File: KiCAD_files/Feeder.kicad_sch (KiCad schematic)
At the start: 82 parts, among them J405 Conn_01x02_Male, J406 Conn_01x02_Male, J501 Conn_01x03, Q501 60V N channel, Q502 TK13P25D,RQ, T501 PA2467NL, U407 OPA316, U501 NCP12700, U502 FODM217A, U503 TL431MFDT,215

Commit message: cleaned refdes
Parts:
- removed C415: 100nF, Footprints:C_0805_2012Metric, symbol Device:C_Small
- removed C503, C504, C505, C506: 4.7uF, Footprints:C_1210_3225Metric, symbol Device:C
- removed C509: 1nF, Footprints:C_0805_2012Metric, symbol Device:C
- removed C512, C513: 1uF, Footprints:C_0805_2012Metric, symbol Device:C
- removed C519: 10uF, Footprints:C_1210_3225Metric, symbol Device:C
- removed R422: 47k, Footprints:R_0805_2012Metric, symbol Device:R
- removed R423: 12k, Footprints:R_0805_2012Metric, symbol Device:R
- removed R502, R518: 27k, Footprints:R_0805_2012Metric, symbol Device:R
- removed R506: 470R, Footprints:R_0805_2012Metric, symbol Device:R
- removed U502: FODM217A, Package_SO:SO-4_4.4x2.3mm_P1.27mm, symbol Isolator:SFH617A-1X007T
- added C? (x2): 1uF, Footprints:C_0805_2012Metric, symbol Device:C_Small
- added C? (x4): 4.7uF, Footprints:C_1210_3225Metric, symbol Device:C
- added C?: 100nF, Footprints:C_0805_2012Metric, symbol Device:C_Small
- added C?: 10uF, Footprints:C_1210_3225Metric, symbol Device:C_Small
- added C?: 1nF, Footprints:C_0805_2012Metric, symbol Device:C_Small
- added R617: 470R, Footprints:R_0805_2012Metric, symbol Device:R_Small
- added R?: 12k, Footprints:R_0805_2012Metric, symbol Device:R_Small
- added R? (x2): 27k, Footprints:R_0805_2012Metric, symbol Device:R_Small
- added R?: 47k, Footprints:R_0805_2012Metric, symbol Device:R_Small
- added U?: FODM217A, Package_SO:SO-4_4.4x2.3mm_P1.27mm, symbol Isolator:SFH617A-2X009T
- C511: value X7T, 100nF -> 100nF; Dielectric (none) -> X7T
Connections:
- net +5V_DGND: now also C?.1, R?.2
- net +6VJP: now also C?.1
- net COMP: now also C?.2, U?.4
- net DGND: now also C?.2, C?.2, R?.1, R?.1
- net MOSS: now also R617.2
- net PGND: now also C?.1, C?.2, C?.2, C?.2, C?.2, R?.1, U?.3
- net VAUX: now also C?.1
- net VBoost: now also C?.1
- net input: now also C?.1, C?.1
- net at C520.2, R517.2, U503.2 (REF): now also R?.2
- net at C414.2, U407.1 (+): now also R?.1, R?.2
- net at R501.2, U501.1 (UVLO): now also R?.2
- net at R514.2, R515.1: now also U?.1
- net at C520.1, R515.2, U503.1 (K): now also U?.2
- net at C510.1, U501.6 (CS): now also R617.1
- new net: C?.1, C?.1, C?.2, C?.2

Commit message: changed LDO 10uF refdes so it is the same as on SPIN
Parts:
- C? (x5): Voltage 50V -> 25V; manf# 12105C106KAT2A -> CL21B106KAYQNNE
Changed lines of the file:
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@@
       (effects (font (size 1.27 1.27)) hide)
     )
-    (property "manf#" "12105C106KAT2A" (at 237.49 251.46 0)
+    (property "manf#" "CL21B106KAYQNNE" (at 237.49 251.46 0)
       (effects (font (size 1.27 1.27)) hide)
     )
@@
       (effects (font (size 1.27 1.27)) hide)
     )
-    (property "Voltage" "50V" (at 237.49 251.46 0)
+    (property "Voltage" "25V" (at 237.49 251.46 0)
       (effects (font (size 1.27 1.27)) hide)
     )
@@
       (effects (font (size 1.27 1.27)) hide)
     )
-    (property "manf#" "12105C106KAT2A" (at 196.85 251.46 0)
+    (property "manf#" "CL21B106KAYQNNE" (at 196.85 251.46 0)
       (effects (font (size 1.27 1.27)) hide)
     )
@@
       (effects (font (size 1.27 1.27)) hide)
     )
-    (property "Voltage" "50V" (at 196.85 251.46 0)
+    (property "Voltage" "25V" (at 196.85 251.46 0)
       (effects (font (size 1.27 1.27)) hide)
     )
@@
       (effects (font (size 1.27 1.27)) hide)
     )
-    (property "manf#" "12105C106KAT2A" (at 182.88 251.46 0)
+    (property "manf#" "CL21B106KAYQNNE" (at 182.88 251.46 0)
       (effects (font (size 1.27 1.27)) hide)
     )
@@
       (effects (font (size 1.27 1.27)) hide)
     )
-    (property "Voltage" "50V" (at 182.88 251.46 0)
+    (property "Voltage" "25V" (at 182.88 251.46 0)
       (effects (font (size 1.27 1.27)) hide)
     )
@@
       (effects (font (size 1.27 1.27)) hide)
     )
-    (property "manf#" "12105C106KAT2A" (at 137.16 250.19 0)
+    (property "manf#" "CL21B106KAYQNNE" (at 137.16 250.19 0)
       (effects (font (size 1.27 1.27)) hide)
     )
@@
       (effects (font (size 1.27 1.27)) hide)
     )
-    (property "Voltage" "50V" (at 137.16 250.19 0)
+    (property "Voltage" "25V" (at 137.16 250.19 0)
       (effects (font (size 1.27 1.27)) hide)
     )
@@
       (effects (font (size 1.27 1.27)) hide)
     )
-    (property "manf#" "12105C106KAT2A" (at 163.83 250.19 0)
+    (property "manf#" "CL21B106KAYQNNE" (at 163.83 250.19 0)
       (effects (font (size 1.27 1.27)) hide)
     )
@@
       (effects (font (size 1.27 1.27)) hide)
     )
-    (property "Voltage" "50V" (at 163.83 250.19 0)
+    (property "Voltage" "25V" (at 163.83 250.19 0)
       (effects (font (size 1.27 1.27)) hide)
     )

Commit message: Version as built for SN001 and SN002
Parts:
- removed R?: 27k, Footprints:R_0805_2012Metric, symbol Device:R_Small
- added R502: 14,7K, Footprints:R_0805_2012Metric, symbol Device:R
- C? (x2): Voltage 25V -> 50V; manf# CL21B106KAYQNNE -> 12105C106KAT2A
- R501: value 348k -> 147K; Package 0805 -> (none); Ref (none) -> ok; manf# CR0805-FX-3483ELF -> CR0805-FX-1473ELF
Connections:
- net PGND: now also R502.2
- net at R501.2, U501.1 (UVLO): now also R502.1
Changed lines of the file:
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@@
   (junction (at 172.72 243.84) (diameter 0) (color 0 0 0 0)
   )
+  (junction (at 77.47 74.93) (diameter 0) (color 0 0 0 0)
+  )
   (junction (at 156.21 60.96) (diameter 0) (color 0 0 0 0)
   )
   (junction (at 198.12 71.12) (diameter 0) (color 0 0 0 0)
   )
-  (junction (at 77.47 74.93) (diameter 0) (color 0 0 0 0)
-  )
   (junction (at 201.93 46.99) (diameter 0) (color 0 0 0 0)
   )
@@
     (stroke (width 0.5) (type default))
   )
+  (wire (pts (xy 77.47 74.93) (xy 77.47 87.63))
+    (stroke (width 0) (type default))
+  )
   (wire (pts (xy 181.61 93.98) (xy 181.61 90.17))
     (stroke (width 0) (type default))
@@
     (stroke (width 0) (type default))
   )
-  (wire (pts (xy 77.47 93.98) (xy 77.47 146.05))
-    (stroke (width 0) (type default))
-  )
   (wire (pts (xy 127 115.57) (xy 127 137.16))
     (stroke (width 0) (type default))
@@
     (stroke (width 0) (type default))
   )
-  (wire (pts (xy 77.47 74.93) (xy 77.47 88.9))
-    (stroke (width 0) (type default))
-  )
   (wire (pts (xy 36.83 46.99) (xy 36.83 59.69))
     (stroke (width 0.45) (type default))
@@
     (stroke (width 0.45) (type default))
   )
+  (wire (pts (xy 77.47 95.25) (xy 77.47 146.05))
+    (stroke (width 0) (type default))
+  )
   (wire (pts (xy 165.1 60.96) (xy 165.1 64.77))
     (stroke (width 0) (type default))
@@
     )
   )
-  (symbol (lib_id "Device:R") (at 77.47 66.04 0) (unit 1)
-    (in_bom yes) (on_board yes) (dnp no) (fields_autoplaced)
-    (property "Reference" "R501" (at 80.01 64.7699 0)
-      (effects (font (size 1.27 1.27)) (justify left))
-    )
-    (property "Value" "348k" (at 80.01 67.3099 0)
-      (effects (font (size 1.27 1.27)) (justify left))
-    )
-    (property "Footprint" "Footprints:R_0805_2012Metric" (at 75.692 66.04 90)
-      (effects (font (size 1.27 1.27)) hide)
-    )
-    (property "Datasheet" "~" (at 77.47 66.04 0)
-      (effects (font (size 1.27 1.27)) hide)
-    )
-    (property "manf#" "CR0805-FX-3483ELF" (at 77.47 66.04 0)
-      (effects (font (size 1.27 1.27)) hide)
-    )
-    (property "Package" "0805" (at 77.47 66.04 0)
-      (effects (font (size 1.27 1.27)) hide)
-    )
-    (pin "1")
-    (pin "2")
-    (instances
-      (project "ownverter"
-        (path "/8d0c1d66-35ef-4a53-a28f-436a11b54f42/bce1534c-362e-45ed-a9dd-a44d6954485a"
-          (reference "R501") (unit 1)
-        )
-      )
-    )
-  )
   (symbol (lib_id "Device:C") (at 36.83 80.01 0) (unit 1)
     (in_bom yes) (on_board yes) (dnp no)
@@
     )
   )
+  (symbol (lib_id "Device:R") (at 77.47 66.04 0) (unit 1)
+    (in_bom yes) (on_board yes) (dnp no) (fields_autoplaced)
+    (property "Reference" "R501" (at 80.01 65.405 0)
+      (effects (font (size 1.27 1.27)) (justify left))
+    )
+    (property "Value" "147K" (at 80.01 67.945 0)
+      (effects (font (size 1.27 1.27)) (justify left))
+    )
+    (property "Footprint" "Footprints:R_0805_2012Metric" (at 75.692 66.04 90)
+      (effects (font (size 1.27 1.27)) hide)
+    )
+    (property "Datasheet" "~" (at 77.47 66.04 0)
+      (effects (font (size 1.27 1.27)) hide)
+    )
+    (property "Manf#" "" (at 77.47 66.04 0)
+      (effects (font (size 1.27 1.27)) hide)
+    )
+    (property "Ref" "ok" (at 77.47 66.04 0)
+      (effects (font (size 1.27 1.27)) hide)
+    )
+    (property "manf#" "CR0805-FX-1473ELF" (at 77.47 66.04 0)
+      (effects (font (size 1.27 1.27)) hide)
+    )
+    (pin "1")
+    (pin "2")
+    (instances
+      (project "ownverter"
+        (path "/8d0c1d66-35ef-4a53-a28f-436a11b54f42/bce1534c-362e-45ed-a9dd-a44d6954485a"
+          (reference "R501") (unit 1)
+        )
+      )
+    )
+  )
   (symbol (lib_id "Device:R") (at 198.12 109.22 0) (unit 1)
     (in_bom yes) (on_board yes) (dnp no) (fields_autoplaced)
@@
     )
   )
-  (symbol (lib_name "R_Small_14") (lib_id "Device:R_Small") (at 77.47 91.44 180) (unit 1)
-    (in_bom yes) (on_board yes) (dnp no)
-    (property "Reference" "R?" (at 83.82 90.17 0)
-      (effects (font (size 1.27 1.27)) (justify left))
-    )
-    (property "Value" "27k" (at 82.55 92.71 0)
-      (effects (font (size 1.27 1.27)) (justify left))
-    )
-    (property "Footprint" "Footprints:R_0805_2012Metric" (at 77.47 91.44 0)
-      (effects (font (size 1.27 1.27)) hide)
-    )
-    (property "Datasheet" "~" (at 77.47 91.44 0)
-      (effects (font (size 1.27 1.27)) hide)
-    )
-    (property "manf#" "CR0805-FX-2702ELF" (at 77.47 91.44 0)
-      (effects (font (size 1.27 1.27)) hide)
-    )
-    (property "Package" "0805" (at 77.47 91.44 0)
-      (effects (font (size 1.27 1.27)) hide)
-    )
-    (pin "1")
-    (pin "2")
-    (instances
-      (project "ownverter"
-        (path "/8d0c1d66-35ef-4a53-a28f-436a11b54f42"
-          (reference "R?") (unit 1)
-        )
-        (path "/8d0c1d66-35ef-4a53-a28f-436a11b54f42/d5d50263-0660-44c8-a20f-043dc430c72e"
-          (reference "R204") (unit 1)
-        )
-        (path "/8d0c1d66-35ef-4a53-a28f-436a11b54f42/bce1534c-362e-45ed-a9dd-a44d6954485a"
-          (reference "R502") (unit 1)
-        )
-      )
-    )
-  )
   (symbol (lib_id "power:PWR_FLAG") (at 71.12 45.72 0) (unit 1)
     (in_bom yes) (on_board yes) (dnp no)
@@
     )
   )
+  (symbol (lib_id "Device:R") (at 77.47 91.44 0) (unit 1)
+    (in_bom yes) (on_board yes) (dnp no) (fields_autoplaced)
+    (property "Reference" "R502" (at 80.01 90.805 0)
+      (effects (font (size 1.27 1.27)) (justify left))
+    )
+    (property "Value" "14,7K" (at 80.01 93.345 0)
+      (effects (font (size 1.27 1.27)) (justify left))
+    )
+    (property "Footprint" "Footprints:R_0805_2012Metric" (at 75.692 91.44 90)
+      (effects (font (size 1.27 1.27)) hide)
+    )
+    (property "Datasheet" "~" (at 77.47 91.44 0)
+      (effects (font (size 1.27 1.27)) hide)
+    )
+    (property "manf#" "CR0805-FX-1472ELF" (at 77.47 91.44 0)
+      (effects (font (size 1.27 1.27)) hide)
+    )
+    (pin "1")
+    (pin "2")
+    (instances
+      (project "ownverter"
+        (path "/8d0c1d66-35ef-4a53-a28f-436a11b54f42/bce1534c-362e-45ed-a9dd-a44d6954485a"
+          (reference "R502") (unit 1)
+        )
+      )
+    )
+  )
   (symbol (lib_id "Device:C") (at 105.41 139.7 0) (unit 1)
     (in_bom yes) (on_board yes) (dnp no)
@@
       (effects (font (size 1.27 1.27)) hide)
     )
-    (property "Dielectric" "X7T" (at 165.1 68.58 0)
-      (effects (font (size 1.27 1.27)) hide)
+    (property "Dielectric" "X7T" (at 171.45 72.39 0)
+      (effects (font (size 1.27 1.27)))
     )
     (pin "1")
@@
       (effects (font (size 1.27 1.27)) hide)
     )
-    (property "manf#" "CL21B106KAYQNNE" (at 137.16 250.19 0)
+    (property "manf#" "12105C106KAT2A" (at 137.16 250.19 0)
       (effects (font (size 1.27 1.27)) hide)
     )
@@
       (effects (font (size 1.27 1.27)) hide)
     )
-    (property "Voltage" "25V" (at 137.16 250.19 0)
+    (property "Voltage" "50V" (at 137.16 250.19 0)
       (effects (font (size 1.27 1.27)) hide)
     )
@@
       (effects (font (size 1.27 1.27)) hide)
     )
-    (property "manf#" "CL21B106KAYQNNE" (at 163.83 250.19 0)
+    (property "manf#" "12105C106KAT2A" (at 163.83 250.19 0)
       (effects (font (size 1.27 1.27)) hide)
     )
@@
       (effects (font (size 1.27 1.27)) hide)
     )
-    (property "Voltage" "25V" (at 163.83 250.19 0)
+    (property "Voltage" "50V" (at 163.83 250.19 0)
       (effects (font (size 1.27 1.27)) hide)
     )

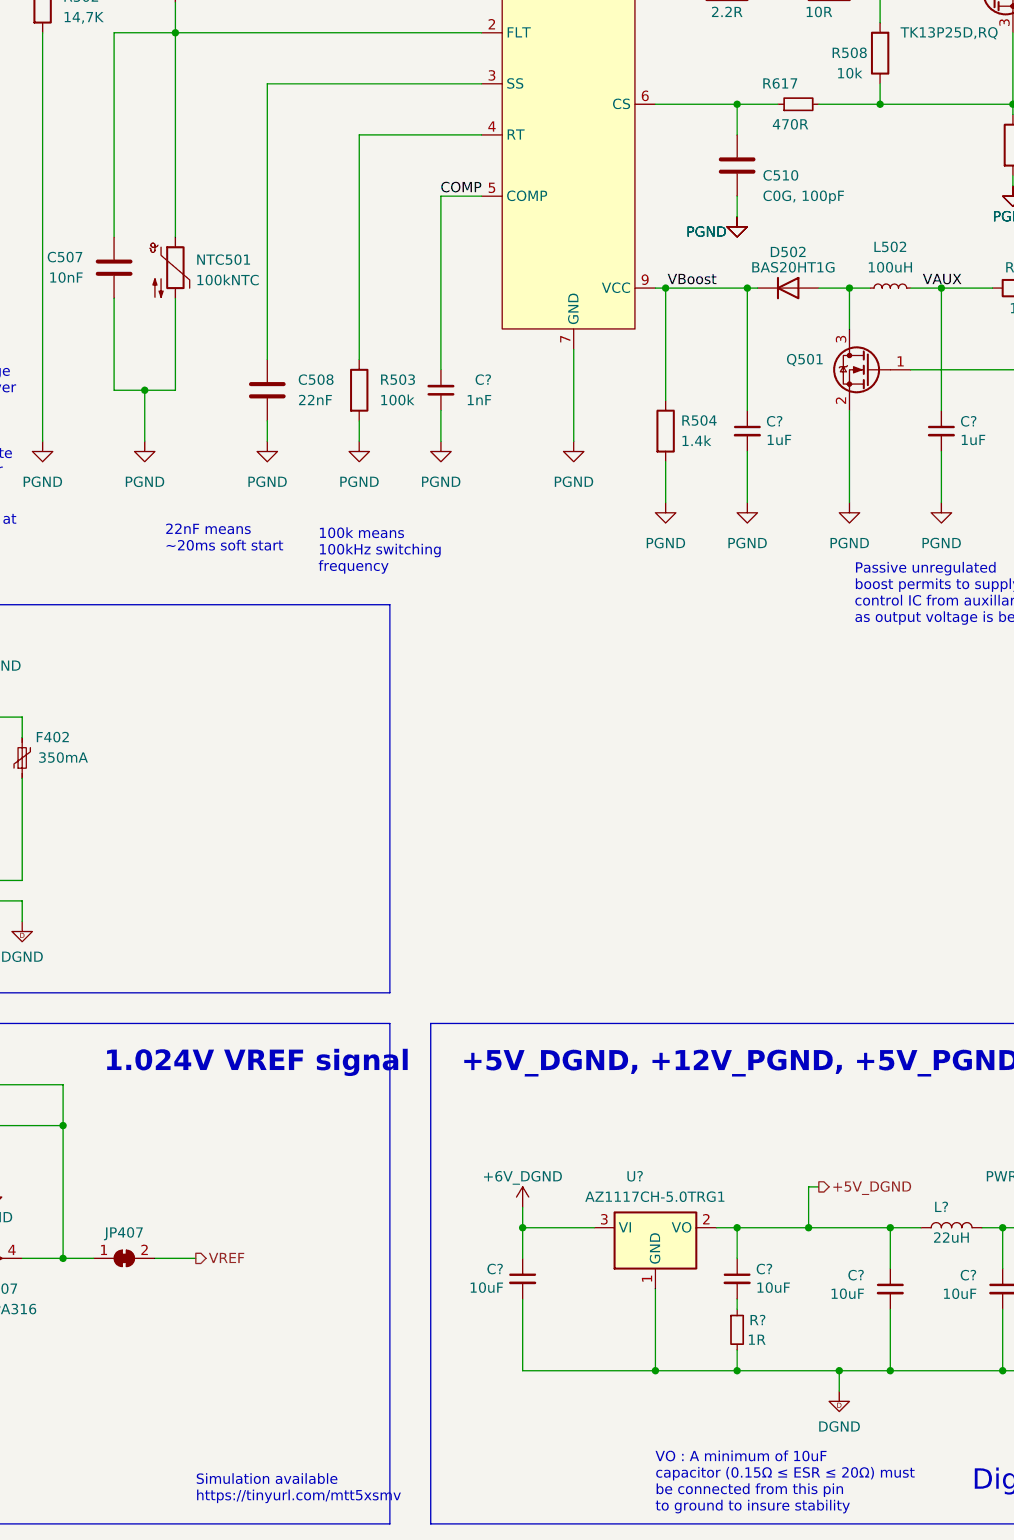
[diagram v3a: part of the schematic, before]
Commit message: cleaned refdes after fabrication of SN001 and SN002
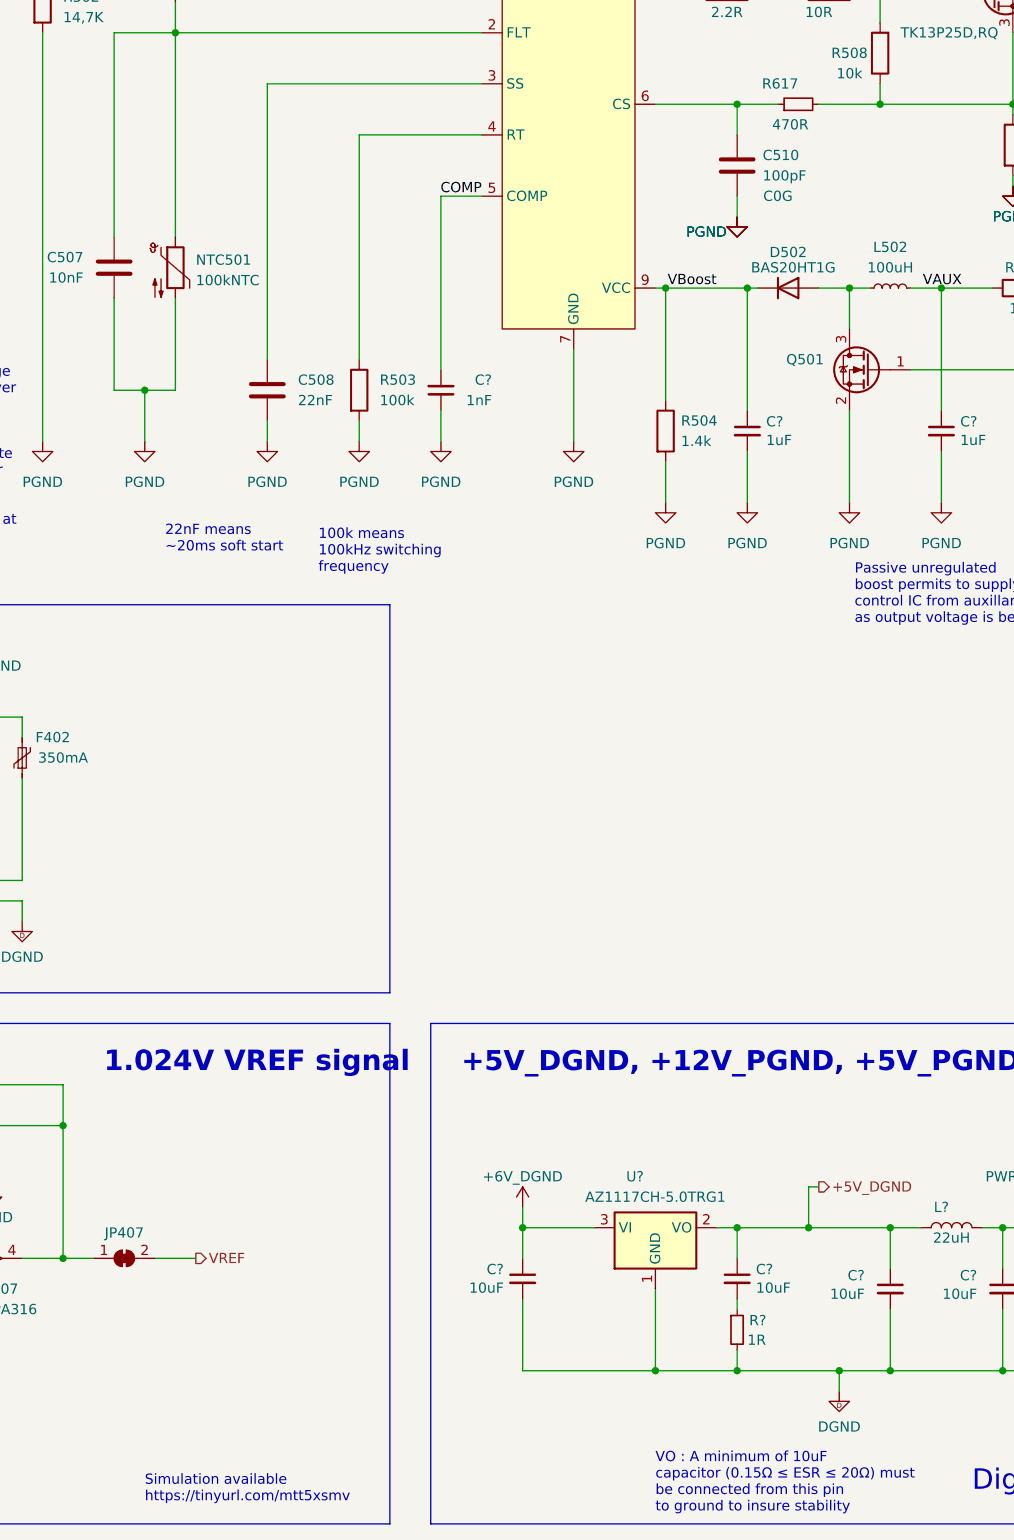
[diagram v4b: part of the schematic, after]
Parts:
- C510: value C0G, 100pF -> 100pF; Dielectric (none) -> C0G
- F401: manf# 0ZCK0035FF2G -> 0ZCH0035FF2G
- F402: manf# 0ZCK0035FF2G -> 0ZCJ0050AF2E
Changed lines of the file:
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@@
     (effects (font (size 1.27 1.27)) (justify left bottom))
   )
-  (text "Simulation available\nhttps://tinyurl.com/mtt5xsmv" (at 96.52 278.13 0)
+  (text "Simulation available\nhttps://tinyurl.com/mtt5xsmv" (at 90.17 278.13 0)
     (effects (font (size 1.27 1.27)) (justify left bottom))
   )
@@
       (effects (font (size 1.27 1.27)) hide)
     )
-    (property "manf#" "0ZCK0035FF2G" (at 74.93 185.42 0)
+    (property "manf#" "0ZCJ0050AF2E" (at 74.93 185.42 0)
       (effects (font (size 1.27 1.27)) hide)
     )
@@
       (effects (font (size 1.27 1.27)) hide)
     )
-    (property "manf#" "0ZCK0035FF2G" (at 64.77 185.42 0)
+    (property "manf#" "0ZCH0035FF2G" (at 64.77 185.42 0)
       (effects (font (size 1.27 1.27)) hide)
     )
@@
   (symbol (lib_id "Device:C") (at 163.83 111.76 0) (unit 1)
     (in_bom yes) (on_board yes) (dnp no)
-    (property "Reference" "C510" (at 167.005 113.03 0)
+    (property "Reference" "C510" (at 167.005 110.49 0)
       (effects (font (size 1.27 1.27)) (justify left))
     )
-    (property "Value" "C0G, 100pF" (at 167.005 115.57 0)
+    (property "Value" "100pF" (at 167.005 113.03 0)
       (effects (font (size 1.27 1.27)) (justify left))
     )
@@
       (effects (font (size 1.27 1.27)) hide)
     )
+    (property "Dielectric" "C0G" (at 168.91 115.57 0)
+      (effects (font (size 1.27 1.27)))
+    )
     (pin "1")
     (pin "2")
@@
       (effects (font (size 1.27 1.27)) hide)
     )
-    (property "Datasheet" "~" (at 311.15 97.79 0)
+    (property "Datasheet" "https://cdn.amphenol-cs.com/media/wysiwyg/files/drawing/10129378.pdf" (at 311.15 97.79 0)
       (effects (font (size 1.27 1.27)) hide)
     )
